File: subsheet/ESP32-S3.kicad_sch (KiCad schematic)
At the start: 14 parts, among them J301 Conn_01x06, SW301 SW_Push, SW302 SW_Push, U301 TLV75533PDBV, U302 ESP32-S3-MINI-1

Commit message: Copy in component arrangement from SDMMC test design
Already had an efficient arrangement for the SPI flash chip, Clock
crystal, and Antenna.
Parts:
- renumbered C301 to C201, C302 to C202, C303 to C203, C304 to C204, C305 to C205, D301 to D201, D302 to D202, J301 to J201, R301 to R201, R302 to R202, SW301 to SW201, SW302 to SW202, U301 to U201, U302 to U202
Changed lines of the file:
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@@
   (symbol (lib_id "power:+5V") (at 62.23 25.4 0) (unit 1)
     (in_bom yes) (on_board yes) (dnp no)
-    (property "Reference" "#PWR0303" (at 62.23 29.21 0)
+    (property "Reference" "#PWR0203" (at 62.23 29.21 0)
       (effects (font (size 1.27 1.27)) hide)
     )
@@
   (symbol (lib_id "power:GND") (at 99.06 38.1 0) (unit 1)
     (in_bom yes) (on_board yes) (dnp no)
-    (property "Reference" "#PWR0308" (at 99.06 44.45 0)
+    (property "Reference" "#PWR0208" (at 99.06 44.45 0)
       (effects (font (size 1.27 1.27)) hide)
     )
@@
   (symbol (lib_id "power:GND") (at 63.5 119.38 0) (unit 1)
     (in_bom yes) (on_board yes) (dnp no)
-    (property "Reference" "#PWR0304" (at 63.5 125.73 0)
+    (property "Reference" "#PWR0204" (at 63.5 125.73 0)
       (effects (font (size 1.27 1.27)) hide)
     )
@@
   (symbol (lib_id "power:GND") (at 162.56 50.8 0) (unit 1)
     (in_bom yes) (on_board yes) (dnp no)
-    (property "Reference" "#PWR0311" (at 162.56 57.15 0)
+    (property "Reference" "#PWR0211" (at 162.56 57.15 0)
       (effects (font (size 1.27 1.27)) hide)
     )
@@
   (symbol (lib_id "Device:C_Small") (at 76.2 97.79 0) (unit 1)
     (in_bom yes) (on_board yes) (dnp no)
-    (property "Reference" "C301" (at 78.5368 96.6216 0)
+    (property "Reference" "C201" (at 78.5368 96.6216 0)
       (effects (font (size 1.27 1.27)) (justify left))
     )
@@
   (symbol (lib_id "Device:LED") (at 243.84 22.86 90) (unit 1)
     (in_bom yes) (on_board yes) (dnp no)
-    (property "Reference" "D302" (at 248.92 24.3205 90)
+    (property "Reference" "D202" (at 248.92 24.3205 90)
       (effects (font (size 1.27 1.27)))
     )
@@
   (symbol (lib_id "power:GND") (at 63.5 147.32 0) (unit 1)
     (in_bom yes) (on_board yes) (dnp no)
-    (property "Reference" "#PWR0305" (at 63.5 153.67 0)
+    (property "Reference" "#PWR0205" (at 63.5 153.67 0)
       (effects (font (size 1.27 1.27)) hide)
     )
@@
   (symbol (lib_id "power:GND") (at 43.18 87.63 0) (unit 1)
     (in_bom yes) (on_board yes) (dnp no)
-    (property "Reference" "#PWR0302" (at 43.18 93.98 0)
+    (property "Reference" "#PWR0202" (at 43.18 93.98 0)
       (effects (font (size 1.27 1.27)) hide)
     )
@@
   (symbol (lib_id "Espressif:ESP32-S3-MINI-1") (at 337.82 132.08 0) (unit 1)
     (in_bom yes) (on_board yes) (dnp no) (fields_autoplaced)
-    (property "Reference" "U302" (at 340.0141 88.9 0)
+    (property "Reference" "U202" (at 340.0141 88.9 0)
       (effects (font (size 1.27 1.27)) (justify left))
     )
@@
   (symbol (lib_id "power:PWR_FLAG") (at 81.28 27.94 0) (unit 1)
     (in_bom yes) (on_board yes) (dnp no) (fields_autoplaced)
-    (property "Reference" "#FLG0301" (at 81.28 26.035 0)
+    (property "Reference" "#FLG0201" (at 81.28 26.035 0)
       (effects (font (size 1.27 1.27)) hide)
     )
@@
   (symbol (lib_id "Device:C_Small") (at 87.63 31.75 0) (unit 1)
     (in_bom yes) (on_board yes) (dnp no)
-    (property "Reference" "C302" (at 85.2932 30.5816 0)
+    (property "Reference" "C202" (at 85.2932 30.5816 0)
       (effects (font (size 1.27 1.27)) (justify right))
     )
@@
   (symbol (lib_id "Device:C_Small") (at 177.8 46.99 0) (unit 1)
     (in_bom yes) (on_board yes) (dnp no)
-    (property "Reference" "C305" (at 180.1368 45.8216 0)
+    (property "Reference" "C205" (at 180.1368 45.8216 0)
       (effects (font (size 1.27 1.27)) (justify left))
     )
@@
   (symbol (lib_id "power:GND") (at 177.8 50.8 0) (unit 1)
     (in_bom yes) (on_board yes) (dnp no)
-    (property "Reference" "#PWR0312" (at 177.8 57.15 0)
+    (property "Reference" "#PWR0212" (at 177.8 57.15 0)
       (effects (font (size 1.27 1.27)) hide)
     )
@@
   (symbol (lib_id "power:GND") (at 76.2 101.6 0) (unit 1)
     (in_bom yes) (on_board yes) (dnp no)
-    (property "Reference" "#PWR0307" (at 76.2 107.95 0)
+    (property "Reference" "#PWR0207" (at 76.2 107.95 0)
       (effects (font (size 1.27 1.27)) hide)
     )
@@
   (symbol (lib_id "Device:R_US") (at 76.2 86.36 0) (unit 1)
     (in_bom yes) (on_board yes) (dnp no)
-    (property "Reference" "R301" (at 77.9272 85.1916 0)
+    (property "Reference" "R201" (at 77.9272 85.1916 0)
       (effects (font (size 1.27 1.27)) (justify left))
     )
@@
   (symbol (lib_id "power:+3V3") (at 128.27 19.05 270) (unit 1)
     (in_bom yes) (on_board yes) (dnp no) (fields_autoplaced)
-    (property "Reference" "#PWR0309" (at 124.46 19.05 0)
+    (property "Reference" "#PWR0209" (at 124.46 19.05 0)
       (effects (font (size 1.27 1.27)) hide)
     )
@@
   (symbol (lib_id "Switch:SW_Push") (at 63.5 111.76 90) (unit 1)
     (in_bom yes) (on_board yes) (dnp no)
-    (property "Reference" "SW301" (at 56.261 111.76 0)
+    (property "Reference" "SW201" (at 56.261 111.76 0)
       (effects (font (size 1.27 1.27)))
     )
@@
   (symbol (lib_id "Device:R_Small_US") (at 243.84 31.75 0) (unit 1)
     (in_bom yes) (on_board yes) (dnp no)
-    (property "Reference" "R302" (at 245.5672 30.5816 0)
+    (property "Reference" "R202" (at 245.5672 30.5816 0)
       (effects (font (size 1.27 1.27)) (justify left))
     )
@@
   (symbol (lib_id "Regulator_Linear:TLV75533PDBV") (at 99.06 30.48 0) (unit 1)
     (in_bom yes) (on_board yes) (dnp no)
-    (property "Reference" "U301" (at 99.06 21.7932 0)
+    (property "Reference" "U201" (at 99.06 21.7932 0)
       (effects (font (size 1.27 1.27)))
     )
@@
   (symbol (lib_id "Device:C_Small") (at 162.56 46.99 0) (unit 1)
     (in_bom yes) (on_board yes) (dnp no)
-    (property "Reference" "C304" (at 164.8968 45.8216 0)
+    (property "Reference" "C204" (at 164.8968 45.8216 0)
       (effects (font (size 1.27 1.27)) (justify left))
     )
@@
   (symbol (lib_id "power:+3V3") (at 76.2 81.28 0) (unit 1)
     (in_bom yes) (on_board yes) (dnp no)
-    (property "Reference" "#PWR0306" (at 76.2 85.09 0)
+    (property "Reference" "#PWR0206" (at 76.2 85.09 0)
       (effects (font (size 1.27 1.27)) hide)
     )
@@
   (symbol (lib_id "Connector_Generic:Conn_01x06") (at 25.4 82.55 0) (mirror y) (unit 1)
     (in_bom yes) (on_board yes) (dnp no) (fields_autoplaced)
-    (property "Reference" "J301" (at 25.4 71.12 0)
+    (property "Reference" "J201" (at 25.4 71.12 0)
       (effects (font (size 1.27 1.27)))
     )
@@
   (symbol (lib_id "power:GND") (at 157.48 154.94 0) (unit 1)
     (in_bom yes) (on_board yes) (dnp no) (fields_autoplaced)
-    (property "Reference" "#PWR0310" (at 157.48 161.29 0)
+    (property "Reference" "#PWR0210" (at 157.48 161.29 0)
       (effects (font (size 1.27 1.27)) hide)
     )
@@
   (symbol (lib_id "power:GND") (at 243.84 36.83 0) (unit 1)
     (in_bom yes) (on_board yes) (dnp no) (fields_autoplaced)
-    (property "Reference" "#PWR0313" (at 243.84 43.18 0)
+    (property "Reference" "#PWR0213" (at 243.84 43.18 0)
       (effects (font (size 1.27 1.27)) hide)
     )
@@
   (symbol (lib_id "Switch:SW_Push") (at 63.5 139.7 90) (unit 1)
     (in_bom yes) (on_board yes) (dnp no)
-    (property "Reference" "SW302" (at 56.261 139.7 0)
+    (property "Reference" "SW202" (at 56.261 139.7 0)
       (effects (font (size 1.27 1.27)))
     )
@@
   (symbol (lib_id "Device:C_Small") (at 109.22 31.75 0) (unit 1)
     (in_bom yes) (on_board yes) (dnp no)
-    (property "Reference" "C303" (at 111.76 31.75 0)
+    (property "Reference" "C203" (at 111.76 31.75 0)
       (effects (font (size 1.27 1.27)) (justify left))
     )
@@
   (symbol (lib_id "power:+3V3") (at 38.1 73.66 0) (unit 1)
     (in_bom yes) (on_board yes) (dnp no)
-    (property "Reference" "#PWR0301" (at 38.1 77.47 0)
+    (property "Reference" "#PWR0201" (at 38.1 77.47 0)
       (effects (font (size 1.27 1.27)) hide)
     )
@@
   (symbol (lib_id "Device:D_Schottky") (at 71.12 27.94 180) (unit 1)
     (in_bom yes) (on_board yes) (dnp no)
-    (property "Reference" "D301" (at 73.66 25.4 0)
-      (effects (font (size 1.27 1.27)) (justify left))
-    )
+    (property "Reference" "D201" (at 73.66 25.4 0)
+      (effects (font (size 1.27 1.27)) (justify left))
+    )

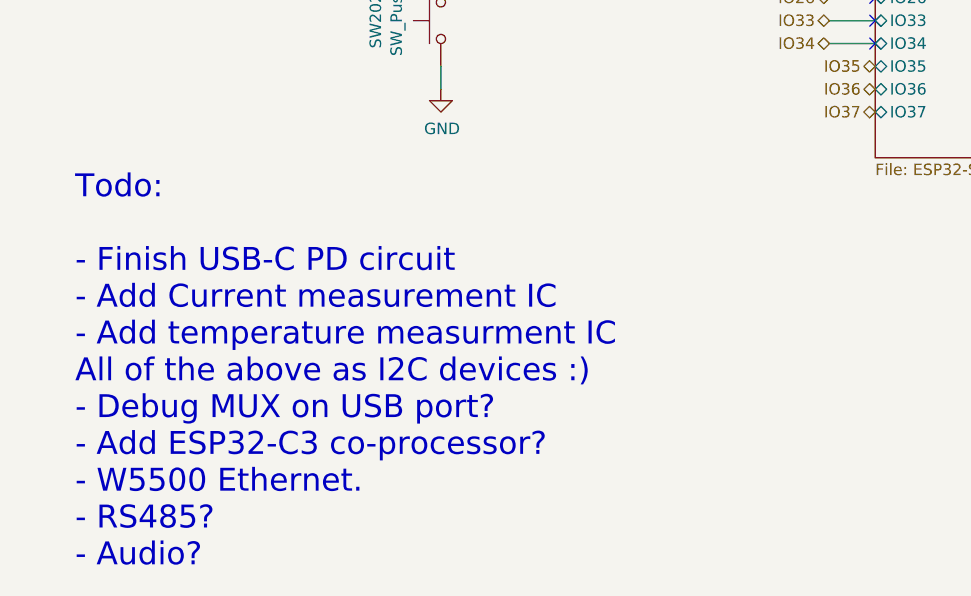
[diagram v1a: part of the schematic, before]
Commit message: Update file format to KiCAD 8.0.0
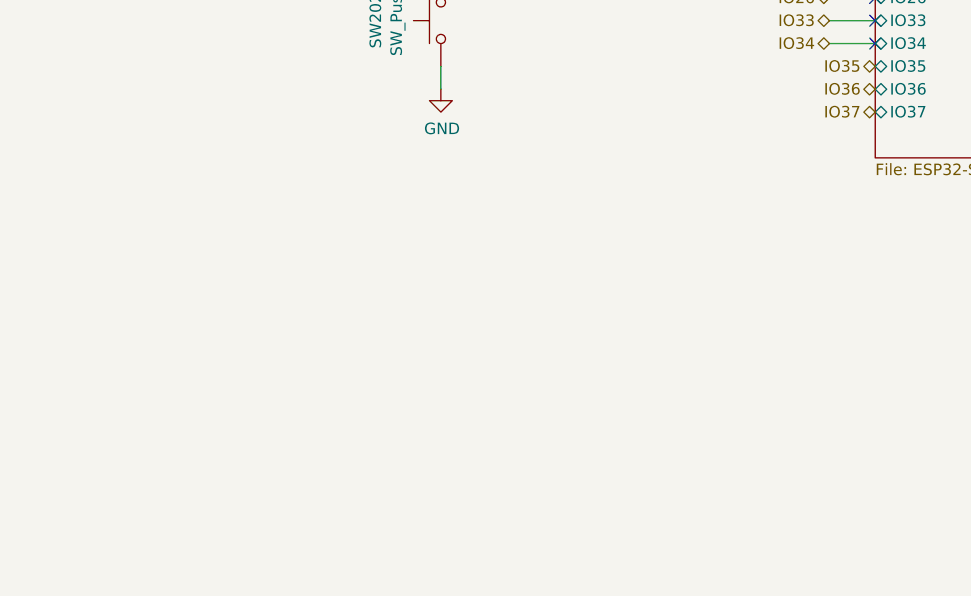
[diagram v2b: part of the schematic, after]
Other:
- note removed: "Todo: - Finish USB-C PD circuit - Add Current measurement IC - Add temperature measurment IC All of the above as I2C devices :) - Debug MUX on USB port? - Add ESP32-C3 co-processor? - W5500 Ethernet. - RS485? - Audio?"

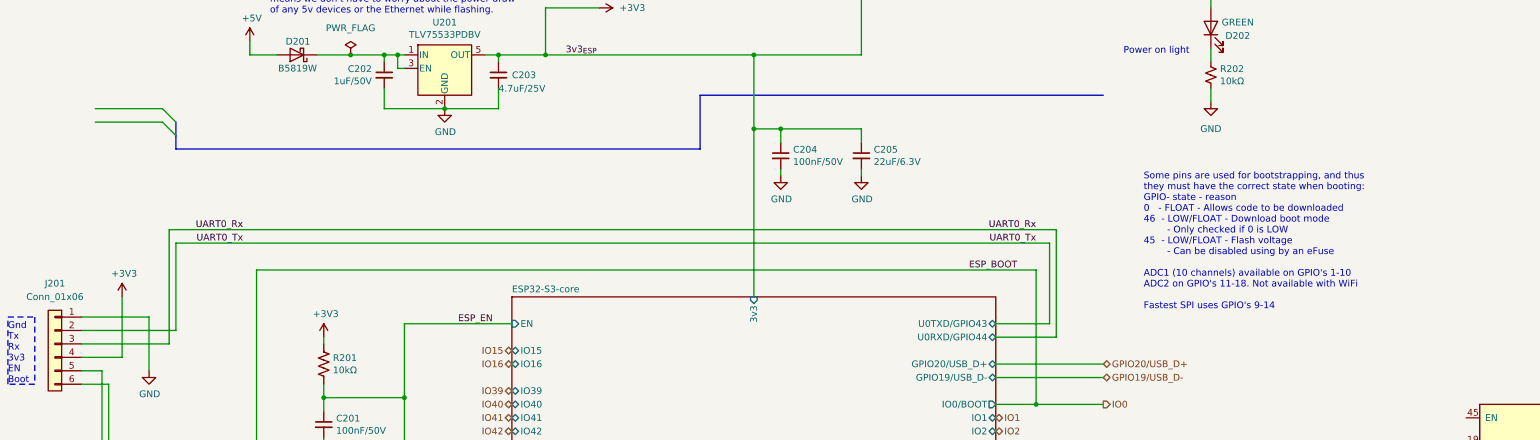
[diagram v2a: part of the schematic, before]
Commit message: Add ESP32-C3 subsheet. SMall corrections
Add and wire up ESP32-C3-Mini on a subsheet, and note down which pins
are used for strapping etc. This will then be replaced with a bare-chip
ESP32-C3 circuit, much like with the existing ESP32-S3 circuit.
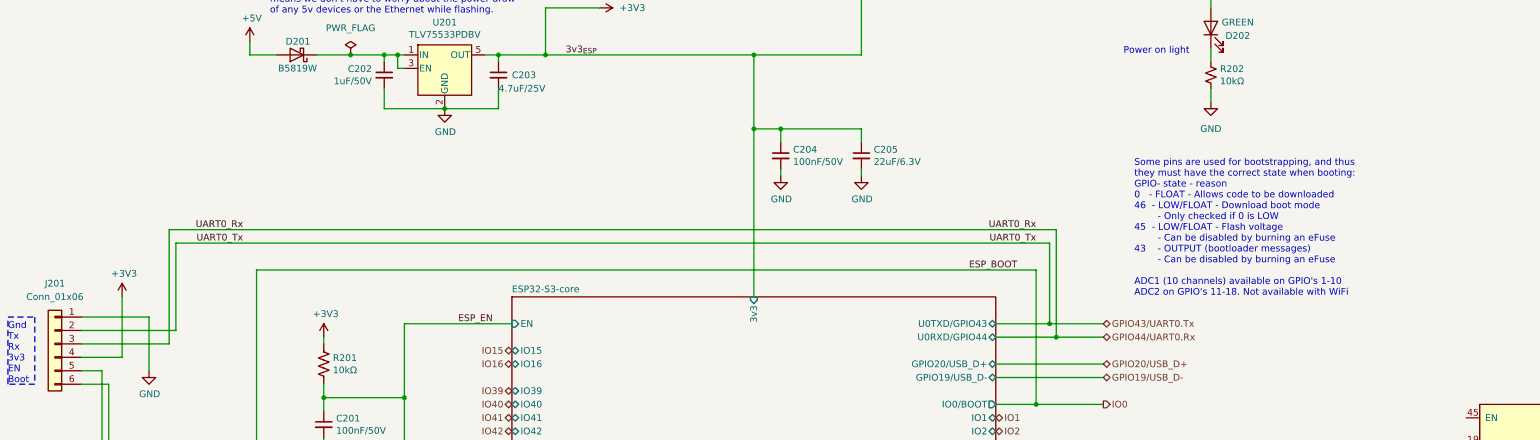
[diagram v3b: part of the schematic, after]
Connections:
- net UART0_Rx renamed GPIO44/UART0.Rx
- net UART0_Tx renamed GPIO43/UART0.Tx
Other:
- note added: "Some pins are used for bootstrapping, and thus they must have the correct state when booting: GPIO- state - reason 0 - FLOAT - Allows code to be downloaded 46 - LOW/FLOAT - Download boot mode - Only checked if 0 is LOW 45 - LOW/FLOAT - Flash voltage - Can be disabled by burning an eFuse 43 - OUTPUT (bootloader messages) - Can be disabled by burning an eFuse ADC1 (10 channels) available on GPIO's 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"
- note removed: "Some pins are used for bootstrapping, and thus they must have the correct state when booting: GPIO- state - reason 0 - FLOAT - Allows code to be downloaded 46 - LOW/FLOAT - Download boot mode - Only checked if 0 is LOW 45 - LOW/FLOAT - Flash voltage - Can be disabled using by an eFuse ADC1 (10 channels) available on GPIO's 1-10 ADC2 on GPIO's 11-18. Not available with WiFi Fastest SPI uses GPIO's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"
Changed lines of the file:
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@@
+	)
+	(junction
+		(at 214.63 81.28)
+		(diameter 0)
+		(color 0 0 0 0)
 	)
 	(junction
@@
 	)
 	(junction
+		(at 213.36 78.74)
+		(diameter 0)
+		(color 0 0 0 0)
+	)
+	(junction
 		(at 157.48 41.91)
 		(diameter 0)
@@
 		(at 111.76 137.16)
 	)
-	(bus_entry
-		(at 45.72 38.1)
-		(size 2.54 2.54)
-		(stroke
-			(width 0)
-			(type default)
-		)
-	)
-	(bus_entry
-		(at 45.72 40.64)
-		(size 2.54 2.54)
-		(stroke
-			(width 0)
-			(type default)
-		)
-	)
 	(wire
 		(pts
@@
 	(wire
 		(pts
-			(xy 33.02 40.64) (xy 45.72 40.64)
-		)
-		(stroke
-			(width 0)
-			(type default)
-		)
-	)
-	(wire
-		(pts
 			(xy 81.28 27.94) (xy 87.63 27.94)
 		)
@@
 		)
 	)
-	(bus
-		(pts
-			(xy 48.26 40.64) (xy 48.26 43.18)
-		)
-		(stroke
-			(width 0)
-			(type default)
-		)
-	)
 	(wire
 		(pts
@@
 	(wire
 		(pts
+			(xy 214.63 81.28) (xy 223.52 81.28)
+		)
+		(stroke
+			(width 0)
+			(type default)
+		)
+	)
+	(wire
+		(pts
 			(xy 157.48 27.94) (xy 157.48 41.91)
 		)
@@
 	(wire
 		(pts
-			(xy 33.02 38.1) (xy 45.72 38.1)
-		)
-		(stroke
-			(width 0)
-			(type default)
-		)
-	)
-	(wire
-		(pts
 			(xy 162.56 44.45) (xy 162.56 41.91)
 		)
@@
 		)
 	)
-	(bus
-		(pts
-			(xy 147.32 35.56) (xy 223.52 35.56)
-		)
-		(stroke
-			(width 0)
-			(type default)
-		)
-	)
 	(wire
 		(pts
@@
 		)
 	)
-	(bus
-		(pts
-			(xy 48.26 45.72) (xy 147.32 45.72)
-		)
-		(stroke
-			(width 0)
-			(type default)
-		)
-	)
-	(bus
-		(pts
-			(xy 48.26 43.18) (xy 48.26 45.72)
-		)
-		(stroke
-			(width 0)
-			(type default)
-		)
-	)
 	(wire
 		(pts
@@
 		)
 	)
-	(bus
-		(pts
-			(xy 147.32 45.72) (xy 147.32 35.56)
-		)
-		(stroke
-			(width 0)
-			(type default)
-		)
-	)
 	(wire
 		(pts
@@
 			(width 0)
 			(type solid)
+		)
+	)
+	(wire
+		(pts
+			(xy 213.36 78.74) (xy 223.52 78.74)
+		)
+		(stroke
+			(width 0)
+			(type default)
 		)
 	)
@@
 		)
 	)
-	(text "Some pins are used for bootstrapping, and thus\nthey must have the correct state when booting:\nGPIO- state - reason\n0   - FLOAT - Allows code to be downloaded\n46  - LOW/FLOAT - Download boot mode\n		- Only checked if 0 is LOW\n45  - LOW/FLOAT - Flash voltage\n		- Can be disabled using by an eFuse\n\nADC1 (10 channels) available on GPIO's 1-10\nADC2 on GPIO's 11-18. Not available with WiFi\n\nFastest SPI uses GPIO's 9-14"
+	(text "Some pins are used for bootstrapping, and thus\nthey must have the correct state when booting:\nGPIO- state - reason\n0   - FLOAT - Allows code to be downloaded\n46  - LOW/FLOAT - Download boot mode\n		- Only checked if 0 is LOW\n45  - LOW/FLOAT - Flash voltage\n		- Can be disabled by burning an eFuse\n43	- OUTPUT (bootloader messages)\n		- Can be disabled by burning an eFuse\n\nADC1 (10 channels) available on GPIO's 1-10\nADC2 on GPIO's 11-18. Not available with WiFi"
 		(exclude_from_sim no)
-		(at 231.14 76.2 0)
+		(at 229.362 73.66 0)
 		(effects
 			(font
@@
 		)
 	)
+	(hierarchical_label "GPIO44{slash}UART0.Rx"
+		(shape bidirectional)
+		(at 223.52 81.28 0)
+		(fields_autoplaced yes)
+		(effects
+			(font
+				(size 1.27 1.27)
+			)
+			(justify left)
+		)
+	)
 	(hierarchical_label "IO12"
 		(shape bidirectional)
@@
 		(fields_autoplaced yes)
 		(effects
+			(font
+				(size 1.27 1.27)
+			)
+			(justify left)
+		)
+	)
+	(hierarchical_label "GPIO43{slash}UART0.Tx"
+		(shape bidirectional)
+		(at 223.52 78.74 0)
+		(fields_autoplaced yes)
+		(effects
